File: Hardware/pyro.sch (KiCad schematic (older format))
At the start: 4 parts, among them J6 Screw_Terminal_01x02, Q1 G1003A

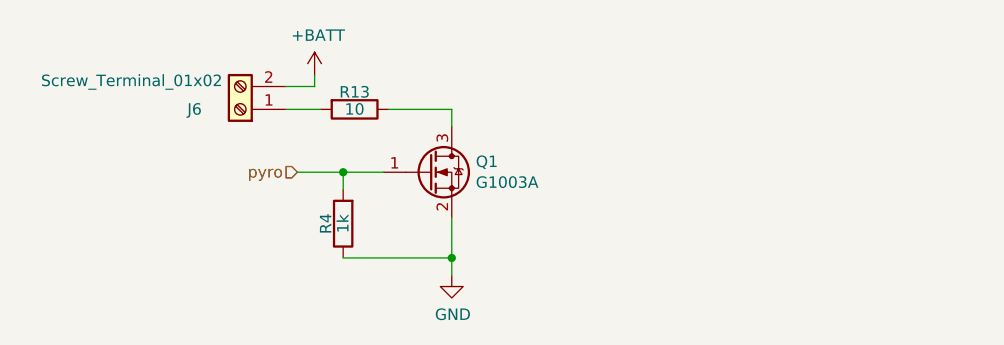
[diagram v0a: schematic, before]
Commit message: Add 2nd pyro, smd headers
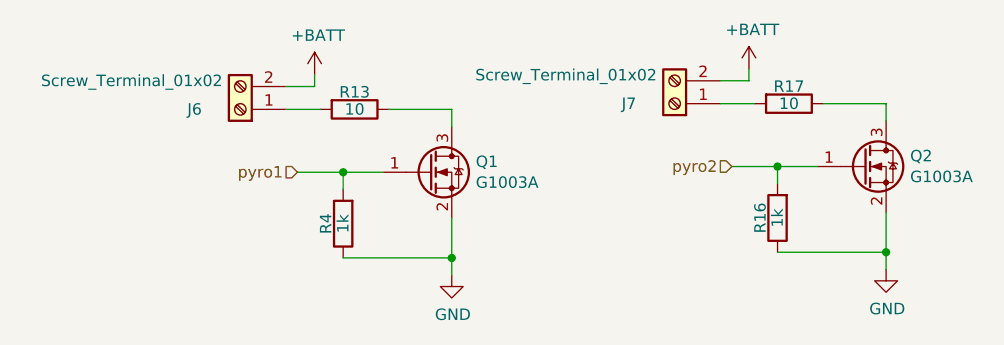
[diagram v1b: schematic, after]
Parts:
- added J7: Screw_Terminal_01x02, TerminalBlock_TE-Connectivity:TerminalBlock_TE_282834-2_1x02_P2.54mm_Horizontal, symbol Connector:Screw_Terminal_01x02
- added Q2: G1003A, Package_TO_SOT_SMD:SOT-23, symbol Device:Q_NMOS_GSD
- added R16: 1k, Resistor_SMD:R_0603_1608Metric, symbol Device:R
- added R17: 10, Resistor_SMD:R_0603_1608Metric, symbol Device:R
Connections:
- net +BATT: now also J7.2 (Pin_2)
- net GND: now also Q2.2 (S), R16.1
- net pyro renamed pyro1
- new net: Q2.3 (D), R17.1
- new net: J7.1 (Pin_1), R17.2
- new net pyro2: Q2.1 (G), R16.2
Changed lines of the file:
@@
 Connection ~ 6475 3625
 Text HLabel 6275 3625 0    50   Input ~ 0
-pyro
+pyro1
 $Comp
 L Connector:Screw_Terminal_01x02 J6
@@
 Wire Wire Line
 	6950 3350 6950 3425
+$Comp
+L Device:R R17
+U 1 1 6116D5D1
+P 8425 3325
+F 0 "R17" V 8350 3325 50  0000 C CNN
+F 1 "10" V 8425 3325 50  0000 C CNN
+F 2 "Resistor_SMD:R_0603_1608Metric" V 8355 3325 50  0001 C CNN
+F 3 "~" H 8425 3325 50  0001 C CNN
+	1    8425 3325
+	0    1    1    0
+$EndComp
+$Comp
+L Device:R R16
+U 1 1 6116D5D7
+P 8375 3825
+F 0 "R16" V 8450 3825 50  0000 C CNN
+F 1 "1k" V 8375 3825 50  0000 C CNN
+F 2 "Resistor_SMD:R_0603_1608Metric" V 8305 3825 50  0001 C CNN
+F 3 "~" H 8375 3825 50  0001 C CNN
+	1    8375 3825
+	-1   0    0    1
+$EndComp
+$Comp
+L Device:Q_NMOS_GSD Q2
+U 1 1 6116D5DD
+P 8750 3600
+F 0 "Q2" H 8955 3646 50  0000 L CNN
+F 1 "G1003A" H 8955 3555 50  0000 L CNN
+F 2 "Package_TO_SOT_SMD:SOT-23" H 8950 3700 50  0001 C CNN
+F 3 "~" H 8750 3600 50  0001 C CNN
+	1    8750 3600
+	1    0    0    -1
+$EndComp
+Wire Wire Line
+	8850 3325 8575 3325
+$Comp
+L power:GND #PWR031
+U 1 1 6116D5E4
+P 8850 4050
+F 0 "#PWR031" H 8850 3800 50  0001 C CNN
+F 1 "GND" H 8855 3877 50  0000 C CNN
+F 2 "" H 8850 4050 50  0001 C CNN
+F 3 "" H 8850 4050 50  0001 C CNN
+	1    8850 4050
+	1    0    0    -1
+$EndComp
+Wire Wire Line
+	8375 3675 8375 3600
+Wire Wire Line
+	8375 3600 8550 3600
+Wire Wire Line
+	8375 3975 8850 3975
+Wire Wire Line
+	8850 3800 8850 3975
+Wire Wire Line
+	8850 3975 8850 4050
+Connection ~ 8850 3975
+Wire Wire Line
+	8175 3600 8375 3600
+Connection ~ 8375 3600
+Text HLabel 8175 3600 0    50   Input ~ 0
+pyro2
+$Comp
+L Connector:Screw_Terminal_01x02 J7
+U 1 1 6116D5F3
+P 7925 3325
+F 0 "J7" H 8125 3325 50  0000 C CNN
+F 1 "Screw_Terminal_01x02" H 8400 3200 50  0000 C CNN
+F 2 "TerminalBlock_TE-Connectivity:TerminalBlock_TE_282834-2_1x02_P2.54mm_Horizontal" H 7925 3325 50  0001 C CNN
+F 3 "~" H 7925 3325 50  0001 C CNN
+	1    7925 3325
+	-1   0    0    1
+$EndComp
+Wire Wire Line
+	8275 3325 8125 3325
+$Comp
+L power:+BATT #PWR030
+U 1 1 6116D5FA
+P 8250 3175
+F 0 "#PWR030" H 8250 3025 50  0001 C CNN
+F 1 "+BATT" H 8265 3348 50  0000 C CNN
+F 2 "" H 8250 3175 50  0001 C CNN
+F 3 "" H 8250 3175 50  0001 C CNN
+	1    8250 3175
+	1    0    0    -1
+$EndComp
+Wire Wire Line
+	8250 3175 8250 3225
+Wire Wire Line
+	8250 3225 8125 3225
+Wire Wire Line
+	8850 3325 8850 3400
 $EndSCHEMATC

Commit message: Change regulator diode footprint, update routing
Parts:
- Q1, Q2: MANUFACTURER (none) -> GOFORD; Manufacturer_Part_Number (none) -> G1003A
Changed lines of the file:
@@
 F 2 "Package_TO_SOT_SMD:SOT-23" H 7050 3725 50  0001 C CNN
 F 3 "~" H 6850 3625 50  0001 C CNN
+F 4 "GOFORD" H 6850 3625 50  0001 C CNN "MANUFACTURER"
+F 5 "G1003A" H 6850 3625 50  0001 C CNN "Manufacturer_Part_Number"
 	1    6850 3625
 	1    0    0    -1
@@
 F 2 "Package_TO_SOT_SMD:SOT-23" H 8950 3700 50  0001 C CNN
 F 3 "~" H 8750 3600 50  0001 C CNN
+F 4 "GOFORD" H 8750 3600 50  0001 C CNN "MANUFACTURER"
+F 5 "G1003A" H 8750 3600 50  0001 C CNN "Manufacturer_Part_Number"
 	1    8750 3600
 	1    0    0    -1
